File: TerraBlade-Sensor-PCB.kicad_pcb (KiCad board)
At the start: 2 copper layers, 96.4 x 95 mm, 21 parts, among them SW1 TS-1187A-B-A-B, U1 XIAO-ESP32-C3-SMD, U2 2.1MHz

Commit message: PCB Design
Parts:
- removed BLADE1: SensorBlade, SensorBlade:SensorBlade_Tenon
- added PAD5: BladePad, Custom:BladePad_SMD, F.Cu at (110.4, 131.7)
- added PAD6: BladePad, Custom:BladePad_SMD, B.Cu at (110.4, 131.7)
- +: renamed from H1; value 2.54-1*4P母 -> -
- R2: value 10K 1% -> 10K
- moved + 42.4 mm to (191.1, 119.3)
- moved H6 42.4 mm to (151.1, 119.3)
- moved R1 19.9 mm to (124.5, 86.0), turned to 180 degrees
- moved LED1 19.7 mm to (124.1, 89.0)
- moved R4 16.8 mm to (135.7, 75.5), turned to 90 degrees
- moved C2 16.1 mm to (117.0, 77.5), turned to -90 degrees
- moved U2 11.1 mm to (112.5, 79.6)
- moved R3 9.42 mm to (135.7, 68.3), turned to -90 degrees
- moved SW1 8.67 mm to (135.3, 85.9)
- moved R5 7.30 mm to (111.7, 73.7), turned to 180 degrees
- moved C1 4.47 mm to (112.4, 85.7), turned to 180 degrees
- moved H2 2.58 mm to (103.5, 73.3)
- moved + 2.50 mm to (143.5, 73.3)
- moved R6 2.36 mm to (116.1, 73.8), turned to 180 degrees
- moved BLADE_SIGNAL 0.42 mm to (123.4, 71.3)
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- renumbered H5 to +, PAD1 to BLADE_SIGNAL, PAD2 to GND
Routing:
- net Net-(SW1-A): track 0.00 -> 41.1 mm, vias 0 -> 2
- net ESP32_D10: track 0.00 -> 40.5 mm, vias 0 -> 2
- net ESP32_D9: track 0.00 -> 39.1 mm, vias 0 -> 2
- net BLADE_SIGNAL: track 0.00 -> 30.4 mm, vias 0 -> 2
- net BAT+: track 0.00 -> 28.8 mm
- net Net-(U1-GPIO2_A0_D0): track 0.00 -> 27.9 mm, vias 0 -> 2
- net Net-(H5-Pad1): track 0.00 -> 26.1 mm
- net Net-(U1-GPIO8_D8_SCK): track 0.00 -> 19.9 mm
- net Net-(H5-Pad2): track 0.00 -> 15.0 mm
- net +3.3V: track 0.00 -> 10.2 mm
- net Net-(U2-DISCH): track 0.00 -> 9.89 mm, vias 0 -> 2
- net GND: track 0.00 -> 3.61 mm, vias 0 -> 3
- net Net-(LED1-K): track 0.00 -> 3.22 mm
- net Net-(U2-CONT): track 0.00 -> 2.88 mm
- added copper zone on B.Cu, net GND
- added copper zone on F.Cu, net GND
- added copper zone on B.Cu, net PROBE_BACK
- added copper zone on F.Cu, net PROBE_FRONT
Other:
- outline, holes or cut-outs redrawn

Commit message: PCB Layout
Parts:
- removed PAD3: PowerPad+, Custom:BladePad_SMD
- removed PAD4: PowerPad-, Custom:BladePad_SMD
- added CN3: PowerPad+, Custom:TESTPOINT-SMD_BD2.0-D1.0-Custom, F.Cu at (162.1, 119.3)
- added CN4: PowerPad-, Custom:TESTPOINT-SMD_BD2.0-D1.0-Custom, F.Cu at (180.1, 119.3)
- +: value - -> 2.54-1*4P母
- R2: value 10K -> 10K 1%
- moved GND 0.14 mm to (123.3, 75.3)
- moved BLADE_SIGNAL 0.11 mm to (123.4, 71.2)
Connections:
- + pad 1: Net-(H5-Pad1) -> POWER_PAD_+
- + pad 2: Net-(H5-Pad2) -> POWER_PAD_-
- + pad 3: unconnected-(H5-Pad3) -> POWER_PAD_-
- + pad 4: unconnected-(H5-Pad4) -> POWER_PAD_-
- H6 pad 1: unconnected-(H6-Pad1) -> POWER_PAD_-
- H6 pad 2: unconnected-(H6-Pad2) -> POWER_PAD_-
- H6 pad 3: unconnected-(H6-Pad3) -> POWER_PAD_-
- H6 pad 4: unconnected-(H6-Pad4) -> POWER_PAD_-
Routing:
- net Net-(H5-Pad1): track 26.1 -> 0.00 mm
- net Net-(H5-Pad2): track 15.0 -> 0.00 mm
- net ESP32_D10: track 40.5 -> 43.7 mm
- net GND: track 3.61 -> 5.32 mm, vias 3 -> 4
- added copper zone on F.Cu, net POWER_PAD_+
- added copper zone on B.Cu, net POWER_PAD_-
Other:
- board text added: "TerraBlade v1.0 V_IN: 3.6V - 4.5V DC (3x AA) SENSOR: 2.1MHz Cap-Osc"

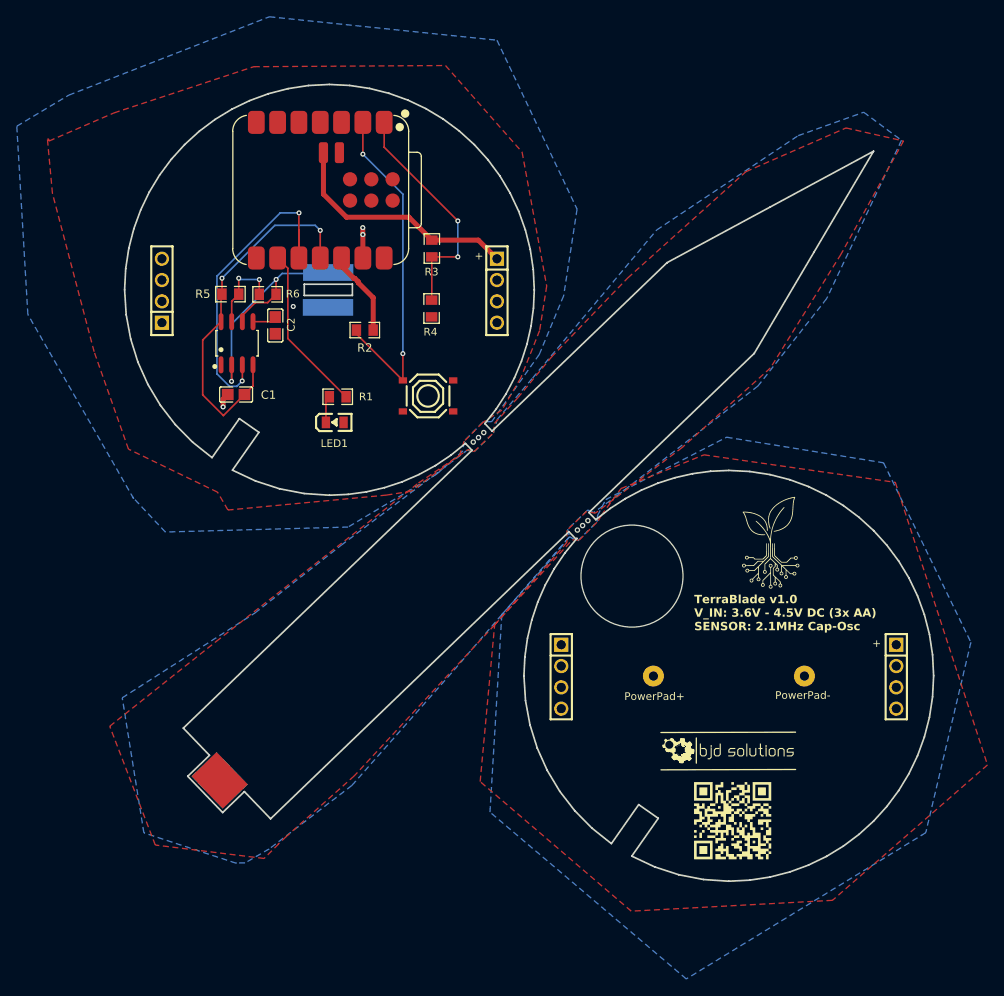
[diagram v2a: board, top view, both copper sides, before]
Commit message: Remap Digital Pins (Don't use strapping pins) / Increase size of the mortise tenon slot
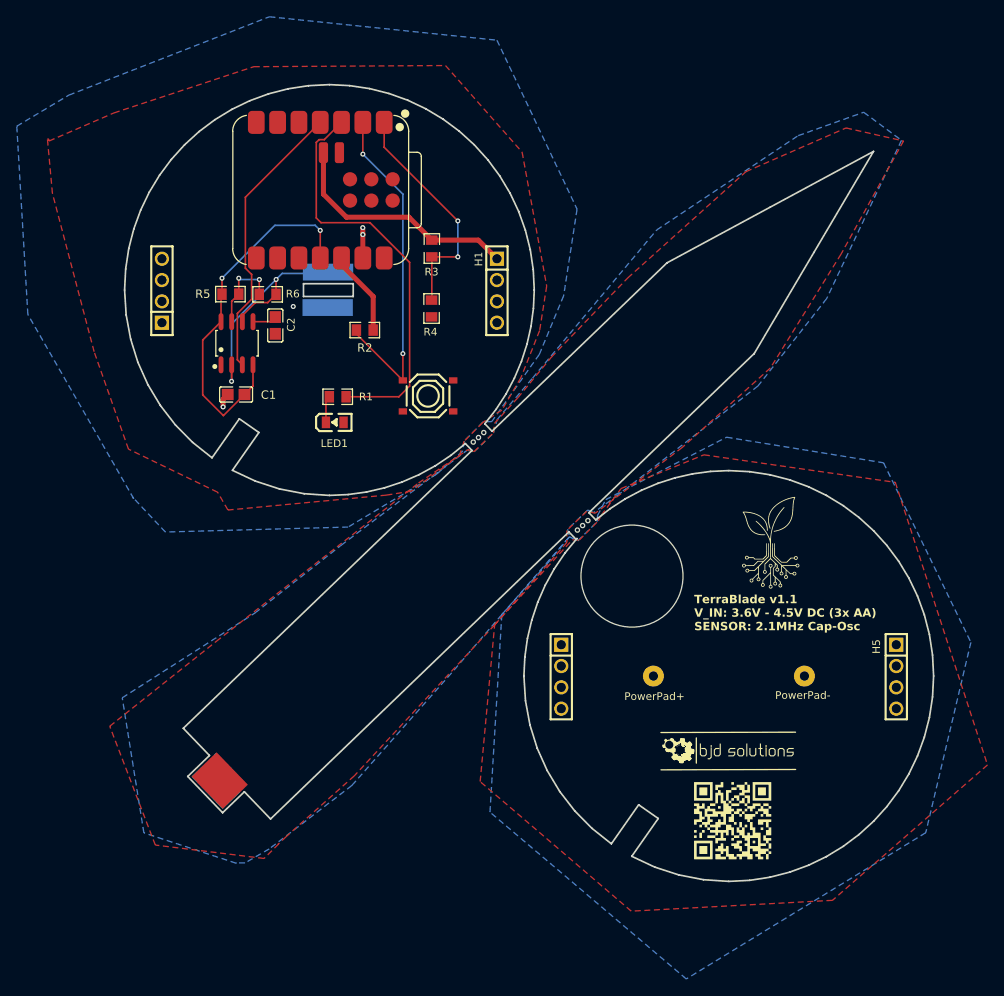
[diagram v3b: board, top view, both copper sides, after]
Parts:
- moved PAD1 0.05 mm to (123.3, 71.1)
- renumbered + to H1, + to H5, BLADE_SIGNAL to PAD1, GND to PAD2
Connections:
- R1 pad 1: Net-(U1-GPIO8_D8_SCK) -> ESP32_D2
- U1 pad 10: ESP32_D9 -> unconnected-(U1-GPIO9_D9_MISO-Pad10)
- U1 pad 3: unconnected-(U1-GPIO4_A2_D2-Pad3) -> ESP32_D2
- U1 pad 4: unconnected-(U1-GPIO5_A3_D3-Pad4) -> ESP32_D3
- U1 pad 9: Net-(U1-GPIO8_D8_SCK) -> unconnected-(U1-GPIO8_D8_SCK-Pad9)
- U2 pad 3: ESP32_D9 -> ESP32_D3
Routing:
- net ESP32_D2: track 0.00 -> 49.2 mm
- net ESP32_D9: track 39.1 -> 0.00 mm, vias 2 -> 0
- net ESP32_D3: track 0.00 -> 33.9 mm
- net Net-(U1-GPIO8_D8_SCK): track 19.9 -> 0.00 mm
- net +3.3V: track 10.2 -> 11.1 mm
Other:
- outline, holes or cut-outs redrawn
- board text added: "TerraBlade v1.1 V_IN: 3.6V - 4.5V DC (3x AA) SENSOR: 2.1MHz Cap-Osc"
- board text removed: "TerraBlade v1.0 V_IN: 3.6V - 4.5V DC (3x AA) SENSOR: 2.1MHz Cap-Osc"

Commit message: Silk Screen changes
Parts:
- renumbered H5 to +, H1 to +, PAD1 to BLADE_SIGNAL, PAD2 to GND
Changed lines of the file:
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@@
 		(layer "F.Cu")
 		(at 191.066 119.335 -90)
-		(property "Reference" "H5"
+		(property "Reference" "+"
 			(at -4.46 1.83 90)
 			(layer "F.SilkS")
@@
 		(layer "F.Cu")
 		(at 143.47 73.33 -90)
-		(property "Reference" "H1"
+		(property "Reference" "+"
 			(at -4.64 1.64 90)
 			(layer "F.SilkS")
@@
 		(layer "B.Cu")
 		(at 123.34 71.11 90)
-		(property "Reference" "PAD1"
+		(property "Reference" "BLADE_SIGNAL"
 			(at 2.4 -0.01 0)
 			(layer "B.SilkS")
@@
 		(layer "B.Cu")
 		(at 123.3 75.34 -90)
-		(property "Reference" "PAD2"
+		(property "Reference" "GND"
 			(at 2.69 -0.05 0)
 			(layer "B.SilkS")
